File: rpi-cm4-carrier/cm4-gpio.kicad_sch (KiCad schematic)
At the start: 23 parts, among them J1 USB4105-GF-A, J2 Micro_SD_Card_Det, U1 74LVC1G07QW5-7, U2 D3V3F4U10LP-7, U3 D3V3F4U10LP-7, U4 BD2233G-GTR, U5 MagJack-A70-112-331N126

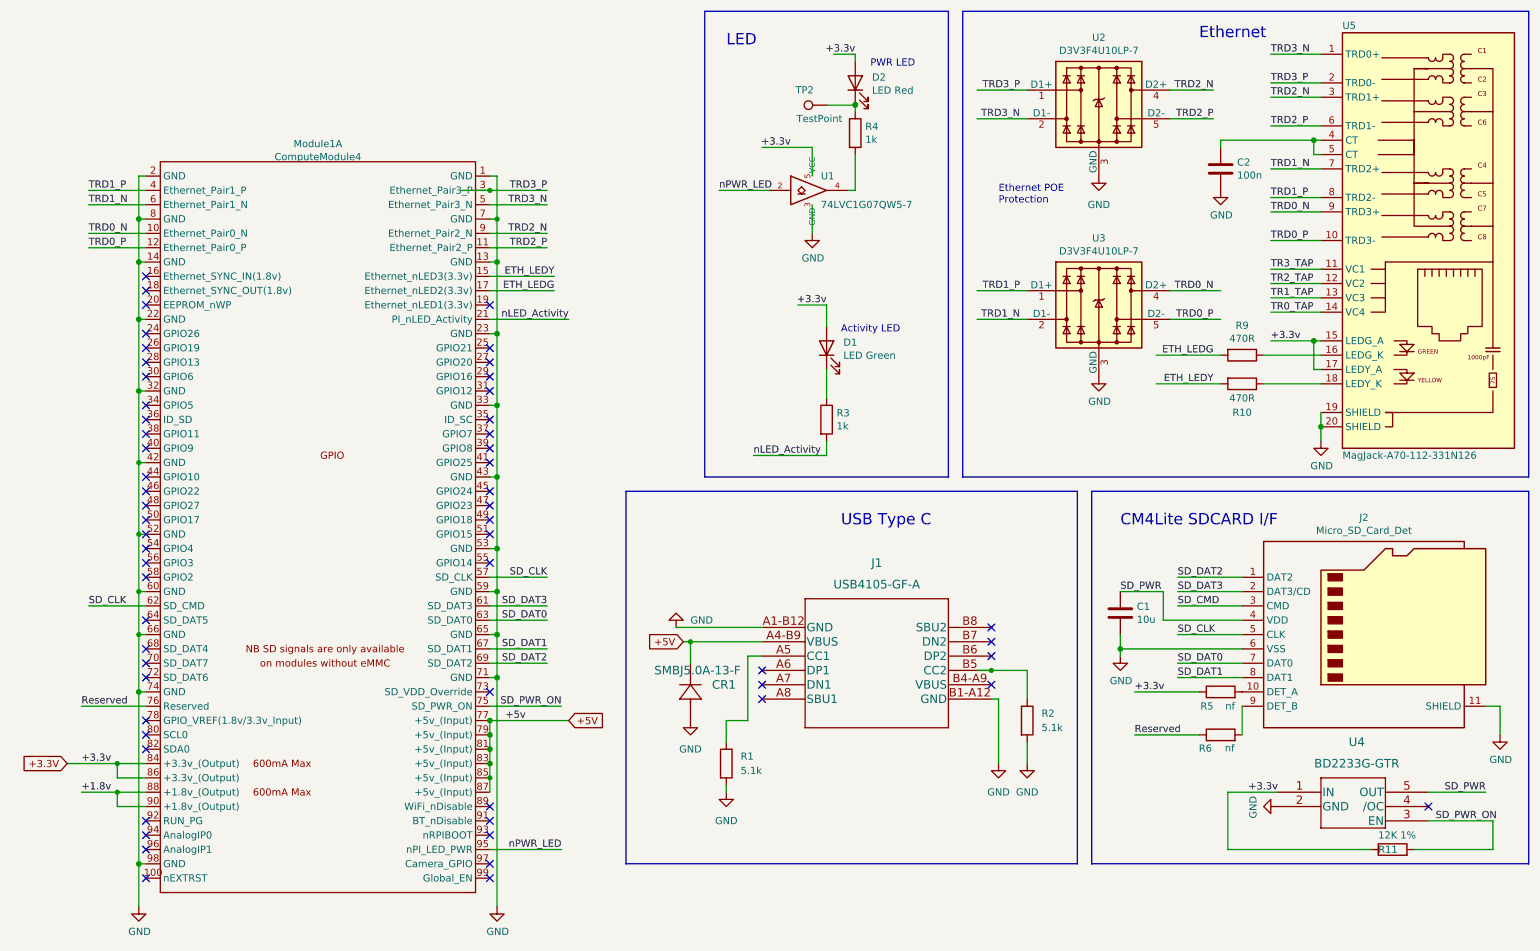
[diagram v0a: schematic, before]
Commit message: Wired Ethernet data
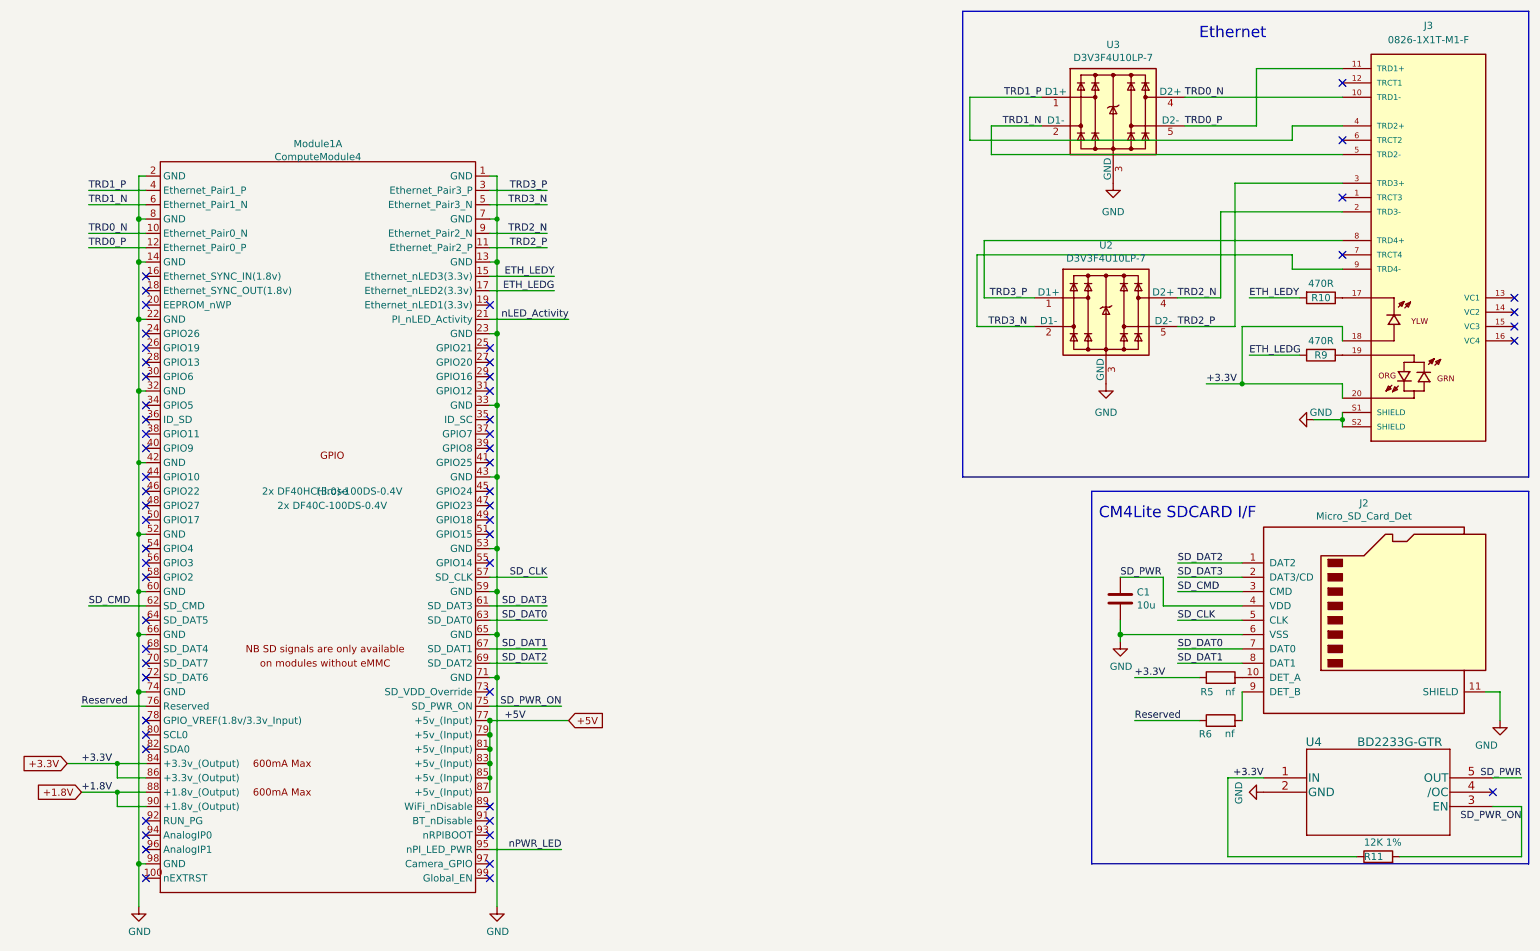
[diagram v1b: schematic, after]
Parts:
- removed C2: 100n, Capacitor_SMD:C_0402_1005Metric, symbol Device:C
- removed CR1: SMBJ5.0A-13-F, SMBJ5.0A-13-F:SMBJ5.0A-13-F, symbol SMBJ5.0A-13-F:SMBJ5.0A-13-F
- removed D1: LED Green, LED_SMD:LED_0603_1608Metric, symbol Device:LED
- removed D2: LED Red, LED_SMD:LED_0603_1608Metric, symbol Device:LED
- removed J1: USB4105-GF-A, USB4105-GF-A:USB4105-GF-A, symbol USB4105-GF-A:USB4105-GF-A
- removed R1, R2: 5.1k, Resistor_SMD:R_0201_0603Metric_Pad0.64x0.40mm_HandSolder, symbol Device:R
- removed R3, R4: 1k, Resistor_SMD:R_0402_1005Metric, symbol Device:R
- removed TP2: TestPoint, TestPoint:TestPoint_Pad_2.0x2.0mm, symbol Connector:TestPoint
- removed U1: 74LVC1G07QW5-7, Package_TO_SOT_SMD:SOT-353_SC-70-5, symbol CM4IO:74LVC1G07_copy
- removed U5: MagJack-A70-112-331N126, CM4IO:TRJG0926HENL, symbol CM4IO:MagJack-A70-112-331N126
- added J3: 0826-1X1T-M1-F, 0826-1X1T-M1-F:0826-1X1T-M1-F, symbol 0826-1X1T-M1-F:0826-1X1T-M1-F
- Module1: Digi-Key_PN (none) -> 2x H11615CT-ND; Digi-Key_PN (Alt) (none) -> 2x H124602CT-ND; MPN (none) -> 2x DF40C-100DS-0.4V; MPN (Alt) (none) -> 2x DF40HC(3.0)-100DS-0.4V; Manufacturer (none) -> Hirose
- U4: footprint BD2233G-GTR:BD2233G-GTR -> Package_TO_SOT_SMD:SOT-23-5
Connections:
- net +3.3V: now also J3.18, J3.20
- net GND: now also J3.S1 (SHIELD), J3.S2 (SHIELD)
- net SD_CLK: no longer Module1.62 (SD_CMD)
- net SD_CMD: now also Module1.62 (SD_CMD)
- net TRD0_N: now also J3.10 (TRD1-)
- net TRD0_P: now also J3.11 (TRD1+)
- net TRD1_N: now also J3.5 (TRD2-)
- net TRD1_P: now also J3.4 (TRD2+)
- net TRD2_N: now also J3.2 (TRD3-)
- net TRD2_P: now also J3.3 (TRD3+)
- net TRD3_N: now also J3.9 (TRD4-)
- net TRD3_P: now also J3.8 (TRD4+)
- net at R9.1: now also J3.19
- net at R10.1: now also J3.17
- net +1.8v renamed +1.8V
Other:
- note removed: "Activity LED"
- note removed: "Ethernet POE Protection"
- note removed: "LED"
- note removed: "PWR LED"
- note removed: "USB Type C"
- moved on the sheet: C1, J2, R10, R11, R5, R6, U2, U3, U4
